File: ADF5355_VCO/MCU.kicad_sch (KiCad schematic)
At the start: 1 part, among them U1 STM32L433RCTx

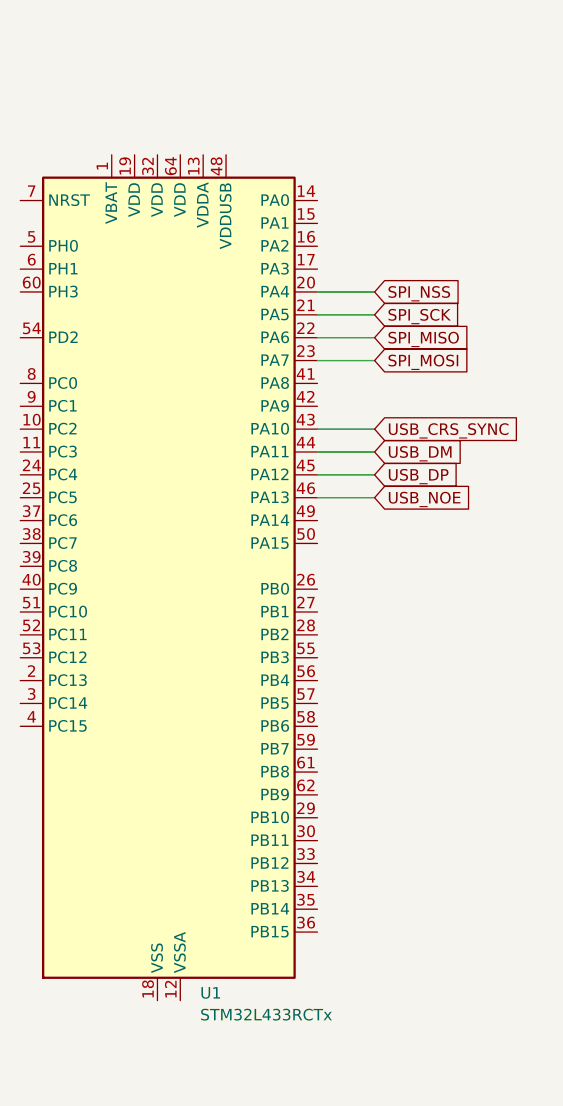
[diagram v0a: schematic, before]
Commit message: ¸Added USB connector and changed connections
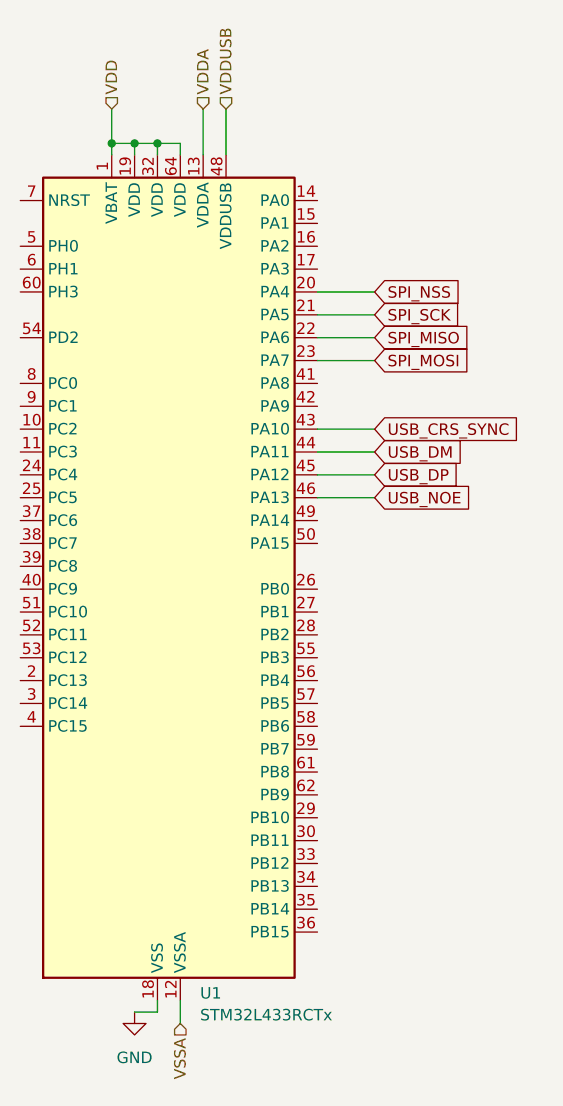
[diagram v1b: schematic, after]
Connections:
- net VDD: now reaches U1.1 (VBAT)
- net VDD: now also U1.19 (VDD), U1.32 (VDD), U1.64 (VDD)
- net VSSA: now reaches U1.12 (VSSA)
- net VDDA: now reaches U1.13 (VDDA)
- net GND: now reaches U1.18 (VSS), U1.31 (VSS), U1.47 (VSS), U1.63 (VSS)
- net VDDUSB: now reaches U1.48 (VDDUSB)
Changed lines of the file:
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@@
 (kicad_sch (version 20230121) (generator eeschema)
   (paper "A4")
+  (junction (at 109.22 44.45) (diameter 0) (color 0 0 0 0)
+  )
+  (junction (at 114.3 44.45) (diameter 0) (color 0 0 0 0)
+  )
+  (junction (at 111.76 44.45) (diameter 0) (color 0 0 0 0)
+  )
+  (wire (pts (xy 111.76 44.45) (xy 111.76 45.72))
+    (stroke (width 0) (type default))
+  )
   (wire (pts (xy 138.43 66.04) (xy 132.08 66.04))
     (stroke (width 0) (type default))
   )
+  (wire (pts (xy 114.3 44.45) (xy 116.84 44.45))
+    (stroke (width 0) (type default))
+  )
   (wire (pts (xy 138.43 63.5) (xy 132.08 63.5))
+    (stroke (width 0) (type default))
+  )
+  (wire (pts (xy 116.84 142.24) (xy 116.84 139.7))
+    (stroke (width 0) (type default))
+  )
+  (wire (pts (xy 119.38 40.64) (xy 119.38 45.72))
+    (stroke (width 0) (type default))
+  )
+  (wire (pts (xy 114.3 140.97) (xy 114.3 139.7))
+    (stroke (width 0) (type default))
+  )
+  (wire (pts (xy 111.76 140.97) (xy 114.3 140.97))
+    (stroke (width 0) (type default))
+  )
+  (wire (pts (xy 116.84 44.45) (xy 116.84 45.72))
+    (stroke (width 0) (type default))
+  )
+  (wire (pts (xy 109.22 44.45) (xy 109.22 45.72))
     (stroke (width 0) (type default))
   )
@@
     (stroke (width 0) (type default))
   )
+  (wire (pts (xy 121.92 40.64) (xy 121.92 45.72))
+    (stroke (width 0) (type default))
+  )
+  (wire (pts (xy 109.22 40.64) (xy 109.22 44.45))
+    (stroke (width 0) (type default))
+  )
   (wire (pts (xy 138.43 78.74) (xy 132.08 78.74))
+    (stroke (width 0) (type default))
+  )
+  (wire (pts (xy 114.3 44.45) (xy 114.3 45.72))
+    (stroke (width 0) (type default))
+  )
+  (wire (pts (xy 109.22 44.45) (xy 111.76 44.45))
     (stroke (width 0) (type default))
   )
@@
   )
   (wire (pts (xy 138.43 83.82) (xy 132.08 83.82))
+    (stroke (width 0) (type default))
+  )
+  (wire (pts (xy 111.76 44.45) (xy 114.3 44.45))
     (stroke (width 0) (type default))
   )
@@
     )
   )
+  (hierarchical_label "VDDA" (shape input) (at 119.38 40.64 90) (fields_autoplaced)
+    (effects (font (size 1.27 1.27)) (justify left))
+  )
+  (hierarchical_label "VSSA" (shape input) (at 116.84 142.24 270) (fields_autoplaced)
+    (effects (font (size 1.27 1.27)) (justify right))
+  )
+  (hierarchical_label "VDDUSB" (shape input) (at 121.92 40.64 90) (fields_autoplaced)
+    (effects (font (size 1.27 1.27)) (justify left))
+  )
+  (hierarchical_label "VDD" (shape input) (at 109.22 40.64 90) (fields_autoplaced)
+    (effects (font (size 1.27 1.27)) (justify left))
+  )
+  (symbol (lib_id "power:GND") (at 111.76 140.97 0) (unit 1)
+    (in_bom yes) (on_board yes) (dnp no) (fields_autoplaced)
+    (property "Reference" "#PWR017" (at 111.76 147.32 0)
+      (effects (font (size 1.27 1.27)) hide)
+    )
+    (property "Value" "GND" (at 111.76 146.05 0)
+      (effects (font (size 1.27 1.27)))
+    )
+    (property "Footprint" "" (at 111.76 140.97 0)
+      (effects (font (size 1.27 1.27)) hide)
+    )
+    (property "Datasheet" "" (at 111.76 140.97 0)
+      (effects (font (size 1.27 1.27)) hide)
+    )
+    (pin "1")
+    (instances
+      (project "ADF5355_VCO"
+        (path "/29349b68-071c-451b-9b1e-10b5ef7e12a6/8e6d62a1-615e-4e74-ad33-9284c4715f87"
+          (reference "#PWR017") (unit 1)
+        )
+      )
+    )
+  )

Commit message: Finished MCU sheet
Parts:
- removed U1: STM32L433RCTx, Package_QFP:LQFP-64_10x10mm_P0.5mm, symbol MCU_ST_STM32L4:STM32L433RCTx
- added C13, C14, C15, C16, C17: C, symbol Device:C
- added C18, C19: 20pF, symbol Device:C_Small
- added C20, C21: 10pF, symbol Device:C_Small
- added C22: 100nF, symbol Device:C_Small
- added D1: Green, symbol Device:LED
- added D2: Red, symbol Device:LED
- added D3: Blue, symbol Device:LED
- added FB1: FerriteBead, symbol Device:FerriteBead
- added R1: 390R, symbol Device:R
- added R10, R11, R12, R13, R14, R15, R16, R17, R18, R19, R2, R20, R3, R4, R5, R6, R7, R8, R9: 10k, symbol Device:R_Small
- added SW2: SW_Push, symbol Switch:SW_Push
- added SW3: SW_DPDT_x2, symbol Switch:SW_DPDT_x2
- added U2: STM32L433CCTx, Package_QFP:LQFP-48_7x7mm_P0.5mm, symbol MCU_ST_STM32L4:STM32L433CCTx
- added Y1: 8MHz, symbol Device:Crystal_Small
- added Y2: 32kHz, symbol Device:Crystal_Small
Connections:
- net GND: now also C13.2, C14.2, C15.2, C16.2, C17.2, C18.1, C19.1, C20.1, C21.1, C22.1, D1.1 (K), D2.1 (K), D3.1 (K), R10.1, R11.1, R14.1, R15.1, R16.1, R17.1, R18.1, R2.1, R3.1, R4.1, R5.1, R6.1, R7.1, R8.1, R9.1, SW2.1, SW3.1 (A), U2.23 (VSS), U2.35 (VSS), U2.47 (VSS), U2.8 (VSSA)
- net SPI_MISO: now also U2.16 (PA6)
- net SPI_MOSI: now also U2.17 (PA7)
- net SPI_NSS: now also U2.14 (PA4)
- net SPI_SCK: now also U2.15 (PA5)
- net USB_DM: now also U2.32 (PA11)
- net USB_DP: now also U2.33 (PA12)
- net VDD: now also C13.1, C14.1, C15.1, C16.1, FB1.1, SW3.3 (C), U2.1 (VBAT), U2.24 (VDD), U2.48 (VDD)
- net VDDA: now also C17.1, FB1.2, U2.9 (VDDA)
- net VDDUSB: now also U2.36 (VDDUSB)
- new net: C19.2, U2.5 (PH0), Y1.1
- new net: C18.2, R1.1, Y1.2
- new net: C21.2, U2.4 (PC15), Y2.2
- new net: R6.2, U2.27 (PB14)
- new net: R19.2, U2.2 (PC13)
- new net: R7.2, U2.28 (PB15)
- new net: R11.2, U2.10 (PA0)
- new net: R20.2, U2.34 (PA13)
- new net: R8.2, U2.18 (PB0)
- new net: R13.2, U2.13 (PA3)
- new net: R16.2, U2.31 (PA10)
- new net: R9.2, U2.19 (PB1)
- new net: R1.2, U2.6 (PH1)
- new net: C20.2, U2.3 (PC14), Y2.1
- new net: R15.2, U2.30 (PA9)
- new net: R10.2, U2.11 (PA1)
- new net: R4.2, U2.25 (PB12)
- new net: R12.2, U2.12 (PA2)
- new net: R17.2, U2.37 (PA14)
- new net: R3.2, U2.22 (PB11)
- new net: R2.2, U2.21 (PB10)
- new net: R18.2, U2.38 (PA15)
- new net: R5.2, U2.26 (PB13)
- new net: R14.2, U2.29 (PA8)
- new net BOOT0_Pin: SW3.2 (B), U2.44 (PH3)
- new net D0: U2.20 (PB2)
- new net D1: U2.39 (PB3)
- new net D2: U2.40 (PB4)
- new net D3: U2.41 (PB5)
- new net D4: U2.42 (PB6)
- new net D5: U2.43 (PB7)
- new net D6: U2.45 (PB8)
- new net D7: U2.46 (PB9)
- new net Reset_pin: C22.2, SW2.2, U2.7 (NRST)
- new net Status_LED_green: D1.2 (A), R12.1
- new net Status_LED_red: D2.2 (A), R13.1
- new net USB_Status: D3.2 (A), R20.1

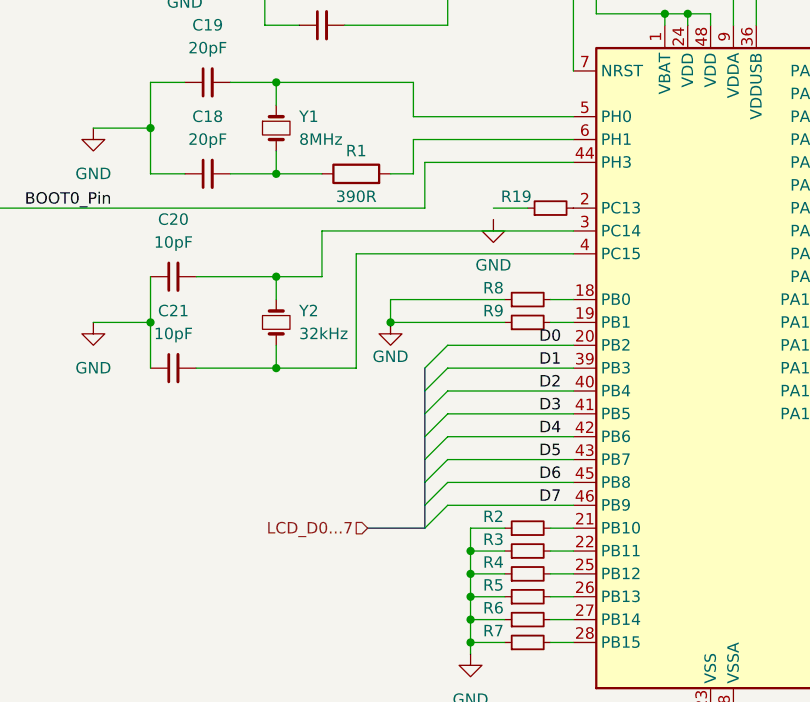
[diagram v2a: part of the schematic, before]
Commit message: Added LCD screen
Added LCD 16x2 screen to the project and modified MCU sheet for using aditional GPIO pins for enable and reset pin.
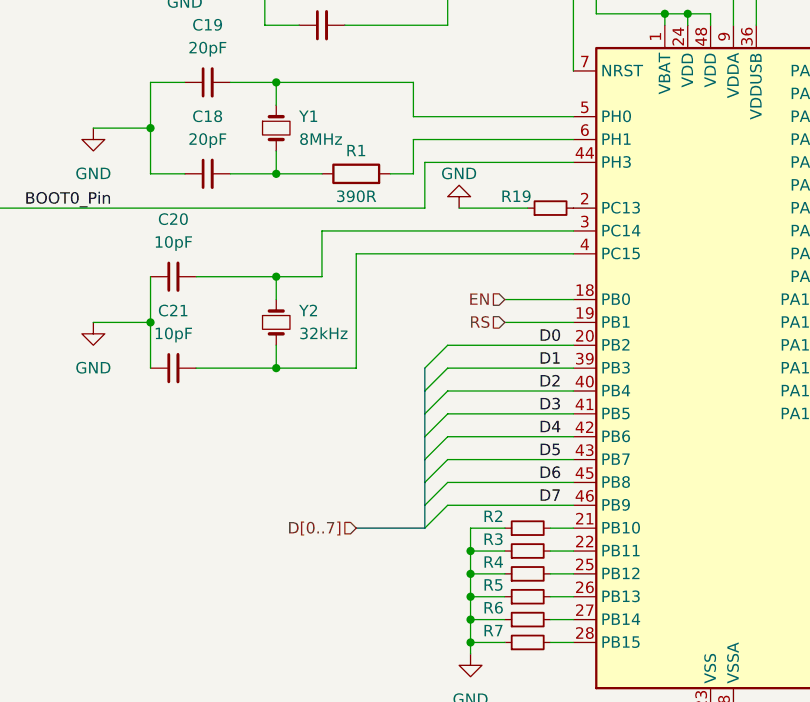
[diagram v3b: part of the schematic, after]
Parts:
- removed R8, R9: 10k, symbol Device:R_Small
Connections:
- net GND: now also R19.1
- net EN: now reaches U2.18 (PB0)
- net RS: now reaches U2.19 (PB1)

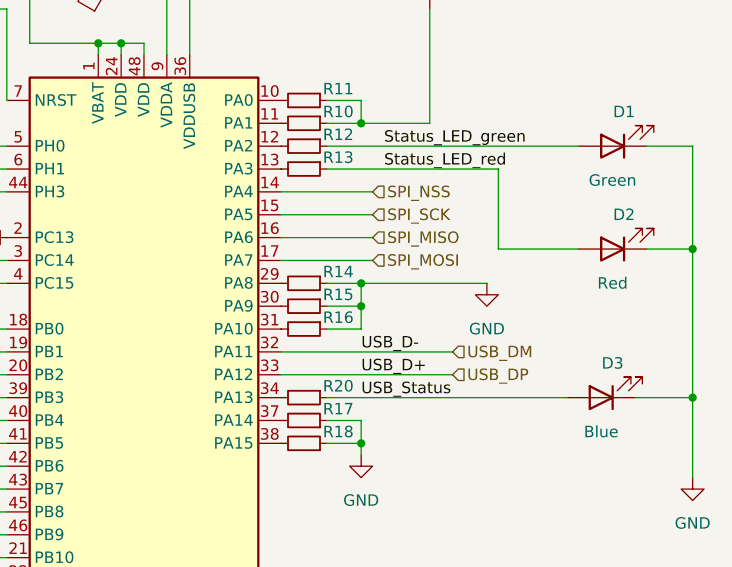
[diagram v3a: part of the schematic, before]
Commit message: Added ADF5355 to the schematic
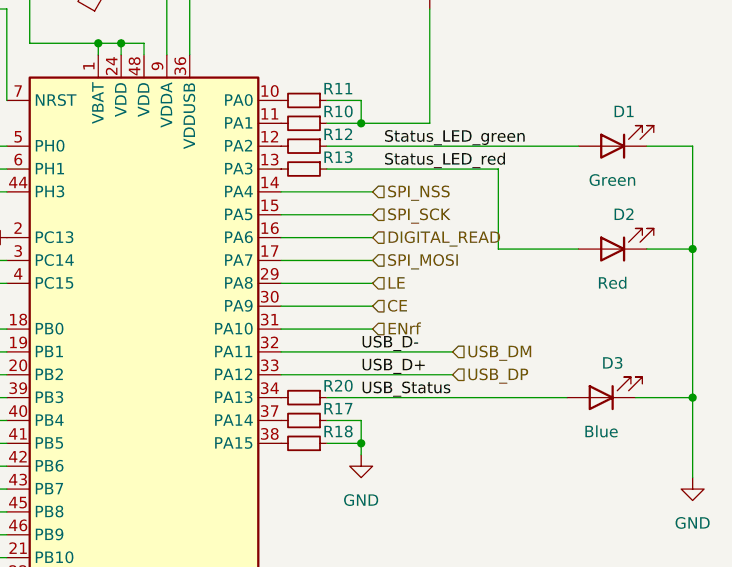
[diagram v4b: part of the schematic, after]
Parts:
- removed R14, R15, R16: 10k, symbol Device:R_Small
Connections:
- net ENrf: now reaches U2.31 (PA10)
- net CE: now reaches U2.30 (PA9)
- net LE: now reaches U2.29 (PA8)
- net SPI_MISO renamed DIGITAL_READ
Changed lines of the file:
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@@
   (junction (at 40.64 165.1) (diameter 0) (color 0 0 0 0)
   )
-  (junction (at 143.51 83.82) (diameter 0) (color 0 0 0 0)
-  )
   (junction (at 92.71 121.92) (diameter 0) (color 0 0 0 0)
   )
@@
   (junction (at 30.48 172.72) (diameter 0) (color 0 0 0 0)
   )
-  (junction (at 143.51 86.36) (diameter 0) (color 0 0 0 0)
-  )
   (bus_entry (at 87.63 114.3) (size 2.54 -2.54)
     (stroke (width 0) (type default))
@@
     (stroke (width 0) (type default))
   )
-  (wire (pts (xy 143.51 86.36) (xy 139.7 86.36))
+  (wire (pts (xy 144.78 83.82) (xy 134.62 83.82))
     (stroke (width 0) (type default))
   )
@@
     (stroke (width 0) (type default))
   )
-  (wire (pts (xy 139.7 88.9) (xy 143.51 88.9))
-    (stroke (width 0) (type default))
-  )
   (wire (pts (xy 90.17 53.34) (xy 104.14 53.34))
     (stroke (width 0) (type default))
@@
     (stroke (width 0) (type default))
   )
-  (wire (pts (xy 143.51 83.82) (xy 157.48 83.82))
-    (stroke (width 0) (type default))
-  )
   (wire (pts (xy 92.71 127) (xy 96.52 127))
     (stroke (width 0) (type default))
@@
     (stroke (width 0) (type default))
   )
-  (wire (pts (xy 143.51 86.36) (xy 143.51 83.82))
-    (stroke (width 0) (type default))
-  )
   (wire (pts (xy 73.66 58.42) (xy 69.85 58.42))
     (stroke (width 0) (type default))
@@
     (stroke (width 0) (type default))
   )
-  (wire (pts (xy 143.51 83.82) (xy 139.7 83.82))
-    (stroke (width 0) (type default))
-  )
   (wire (pts (xy 99.06 78.74) (xy 91.44 78.74))
     (stroke (width 0) (type default))
@@
     (stroke (width 0) (type default))
   )
+  (wire (pts (xy 144.78 86.36) (xy 134.62 86.36))
+    (stroke (width 0) (type default))
+  )
   (wire (pts (xy 90.17 104.14) (xy 104.14 104.14))
     (stroke (width 0) (type default))
@@
     (stroke (width 0) (type default))
   )
-  (wire (pts (xy 143.51 86.36) (xy 143.51 88.9))
-    (stroke (width 0) (type default))
-  )
   (wire (pts (xy 92.71 124.46) (xy 96.52 124.46))
     (stroke (width 0) (type default))
@@
   )
   (wire (pts (xy 180.34 80.01) (xy 180.34 96.52))
+    (stroke (width 0) (type default))
+  )
+  (wire (pts (xy 144.78 88.9) (xy 134.62 88.9))
     (stroke (width 0) (type default))
   )
@@
     (effects (font (size 1.27 1.27)) (justify left bottom))
   )
-  (hierarchical_label "SPI_MISO" (shape input) (at 144.78 78.74 0) (fields_autoplaced)
+  (hierarchical_label "DIGITAL_READ" (shape input) (at 144.78 78.74 0) (fields_autoplaced)
     (effects (font (size 1.27 1.27)) (justify left))
   )
@@
     (effects (font (size 1.27 1.27)) (justify right))
   )
+  (hierarchical_label "ENrf" (shape input) (at 144.78 88.9 0) (fields_autoplaced)
+    (effects (font (size 1.27 1.27)) (justify left))
+  )
   (hierarchical_label "VDD" (shape input) (at 30.48 162.56 90) (fields_autoplaced)
+    (effects (font (size 1.27 1.27)) (justify left))
+  )
+  (hierarchical_label "CE" (shape input) (at 144.78 86.36 0) (fields_autoplaced)
+    (effects (font (size 1.27 1.27)) (justify left))
+  )
+  (hierarchical_label "LE" (shape input) (at 144.78 83.82 0) (fields_autoplaced)
     (effects (font (size 1.27 1.27)) (justify left))
   )
@@
     )
   )
-  (symbol (lib_id "power:GND") (at 157.48 83.82 0) (unit 1)
-    (in_bom yes) (on_board yes) (dnp no) (fields_autoplaced)
-    (property "Reference" "#PWR027" (at 157.48 90.17 0)
-      (effects (font (size 1.27 1.27)) hide)
-    )
-    (property "Value" "GND" (at 157.48 88.9 0)
-      (effects (font (size 1.27 1.27)))
-    )
-    (property "Footprint" "" (at 157.48 83.82 0)
-      (effects (font (size 1.27 1.27)) hide)
-    )
-    (property "Datasheet" "" (at 157.48 83.82 0)
-      (effects (font (size 1.27 1.27)) hide)
-    )
-    (pin "1")
-    (instances
-      (project "ADF5355_VCO"
-        (path "/29349b68-071c-451b-9b1e-10b5ef7e12a6/8e6d62a1-615e-4e74-ad33-9284c4715f87"
-          (reference "#PWR027") (unit 1)
-        )
-      )
-    )
-  )
   (symbol (lib_id "power:GND") (at 24.13 81.28 0) (unit 1)
     (in_bom yes) (on_board yes) (dnp no) (fields_autoplaced)
@@
         (path "/29349b68-071c-451b-9b1e-10b5ef7e12a6/8e6d62a1-615e-4e74-ad33-9284c4715f87"
           (reference "#PWR09") (unit 1)
-        )
-      )
-    )
-  )
-  (symbol (lib_id "Device:R_Small") (at 137.16 88.9 270) (unit 1)
-    (in_bom yes) (on_board yes) (dnp no)
-    (property "Reference" "R16" (at 140.97 87.63 90)
-      (effects (font (size 1.27 1.27)))
-    )
-    (property "Value" "10k" (at 137.16 91.44 90)
-      (effects (font (size 1.27 1.27)) hide)
-    )
-    (property "Footprint" "" (at 137.16 88.9 0)
-      (effects (font (size 1.27 1.27)) hide)
-    )
-    (property "Datasheet" "~" (at 137.16 88.9 0)
-      (effects (font (size 1.27 1.27)) hide)
-    )
-    (pin "1")
-    (pin "2")
-    (instances
-      (project "ADF5355_VCO"
-        (path "/29349b68-071c-451b-9b1e-10b5ef7e12a6/8e6d62a1-615e-4e74-ad33-9284c4715f87"
-          (reference "R16") (unit 1)
         )
       )
@@
         (path "/29349b68-071c-451b-9b1e-10b5ef7e12a6/8e6d62a1-615e-4e74-ad33-9284c4715f87"
           (reference "Y2") (unit 1)
-        )
-      )
-    )
-  )
-  (symbol (lib_id "Device:R_Small") (at 137.16 86.36 270) (unit 1)
-    (in_bom yes) (on_board yes) (dnp no)
-    (property "Reference" "R15" (at 140.97 85.09 90)
-      (effects (font (size 1.27 1.27)))
-    )
-    (property "Value" "10k" (at 137.16 88.9 90)
-      (effects (font (size 1.27 1.27)) hide)
-    )
-    (property "Footprint" "" (at 137.16 86.36 0)
-      (effects (font (size 1.27 1.27)) hide)
-    )
-    (property "Datasheet" "~" (at 137.16 86.36 0)
-      (effects (font (size 1.27 1.27)) hide)
-    )
-    (pin "1")
-    (pin "2")
-    (instances
-      (project "ADF5355_VCO"
-        (path "/29349b68-071c-451b-9b1e-10b5ef7e12a6/8e6d62a1-615e-4e74-ad33-9284c4715f87"
-          (reference "R15") (unit 1)
         )
       )
@@
         )
       )
-    )
-  )
-  (symbol (lib_id "Device:R_Small") (at 137.16 83.82 270) (unit 1)
-    (in_bom yes) (on_board yes) (dnp no)
-    (property "Reference" "R14" (at 140.97 82.55 90)
-      (effects (font (size 1.27 1.27)))
-    )
-    (property "Value" "10k" (at 137.16 86.36 90)
-      (effects (font (size 1.27 1.27)) hide)
-    )
-    (property "Footprint" "" (at 137.16 83.82 0)
-      (effects (font (size 1.27 1.27)) hide)
-    )
-    (property "Datasheet" "~" (at 137.16 83.82 0)
-      (effects (font (size 1.27 1.27)) hide)
-    )
-    (pin "1")
-    (pin "2")
-    (instances
-      (project "ADF5355_VCO"
-        (path "/29349b68-071c-451b-9b1e-10b5ef7e12a6/8e6d62a1-615e-4e74-ad33-9284c4715f87"
-          (reference "R14") (unit 1)
-        )
-      )
